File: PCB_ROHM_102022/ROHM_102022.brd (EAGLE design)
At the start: 152.4 x 142.2 mm, 126 parts, among them IC1 AMS1117-1.8, IC10 TXB0108PWR, IC2 TXB0108PWR, IC3 W9825G6KH-6I, IC4 AMS1117-1.8, IC5 AMS1117-1.8, IC7 TXB0108PWR, J1 2985-6004, J2 2985-6004, J3 2985-6004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

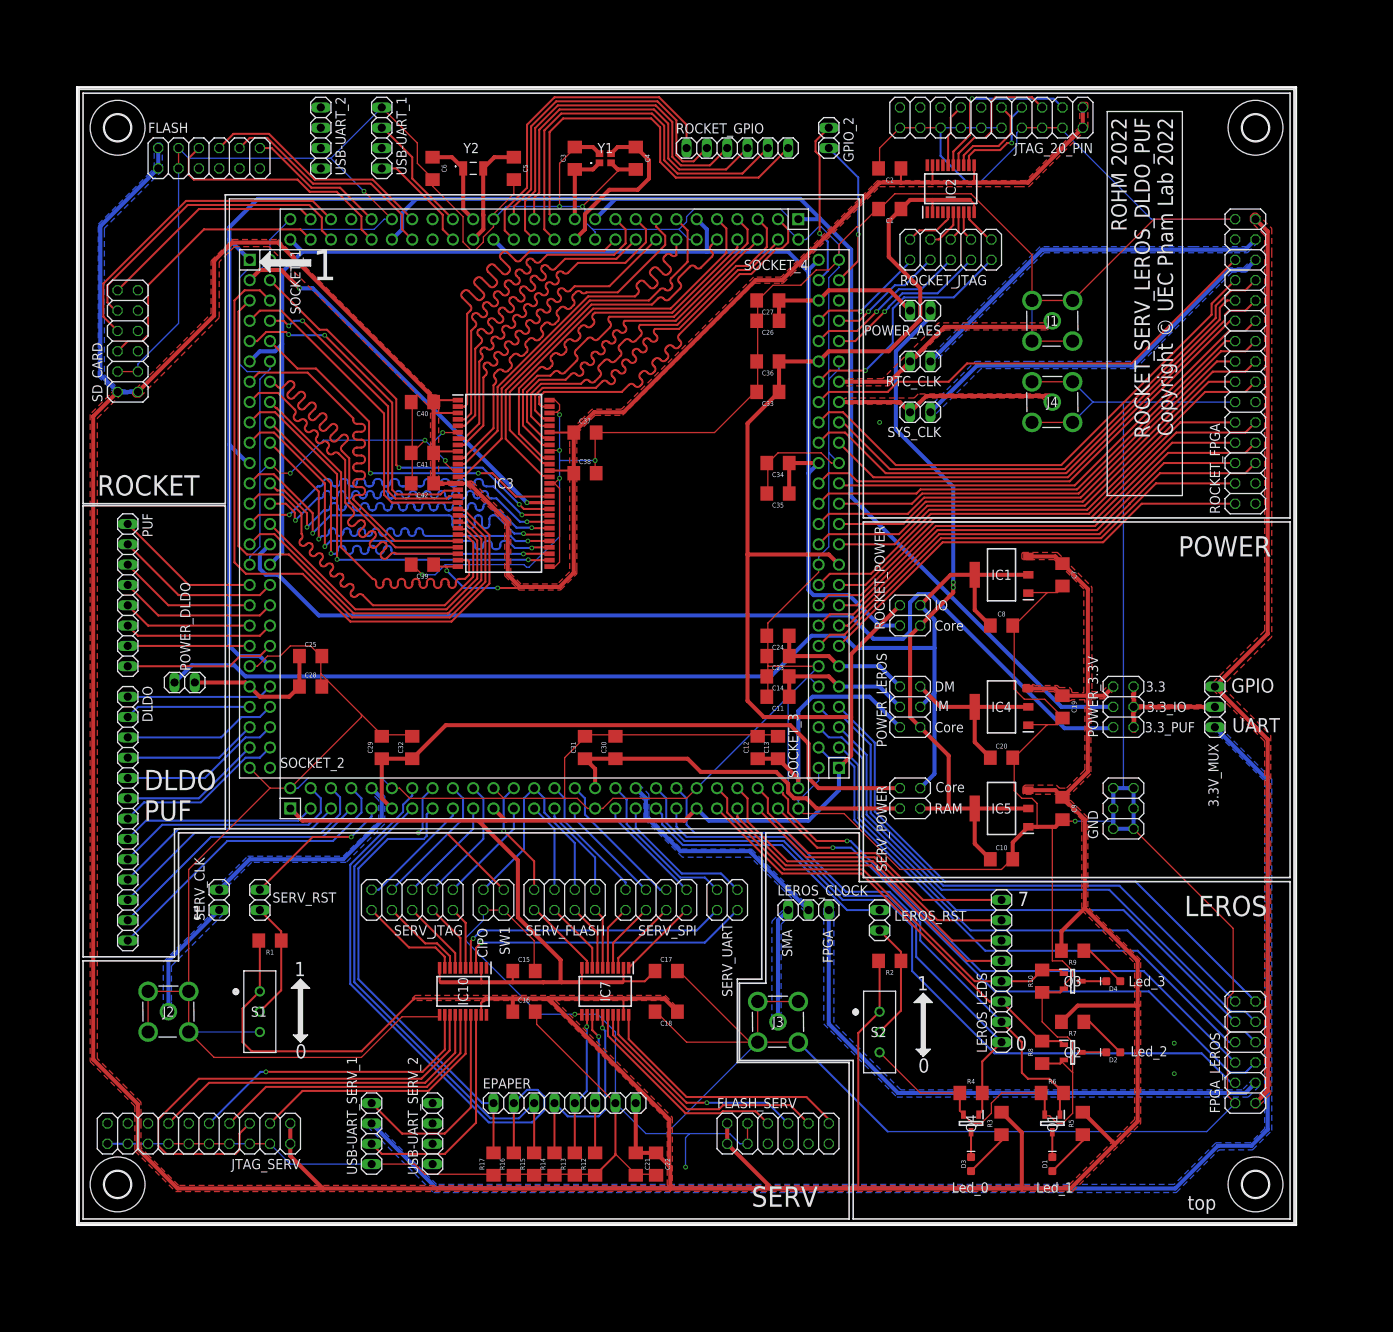
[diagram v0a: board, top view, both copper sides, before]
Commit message: Connect JTAG to FPGA
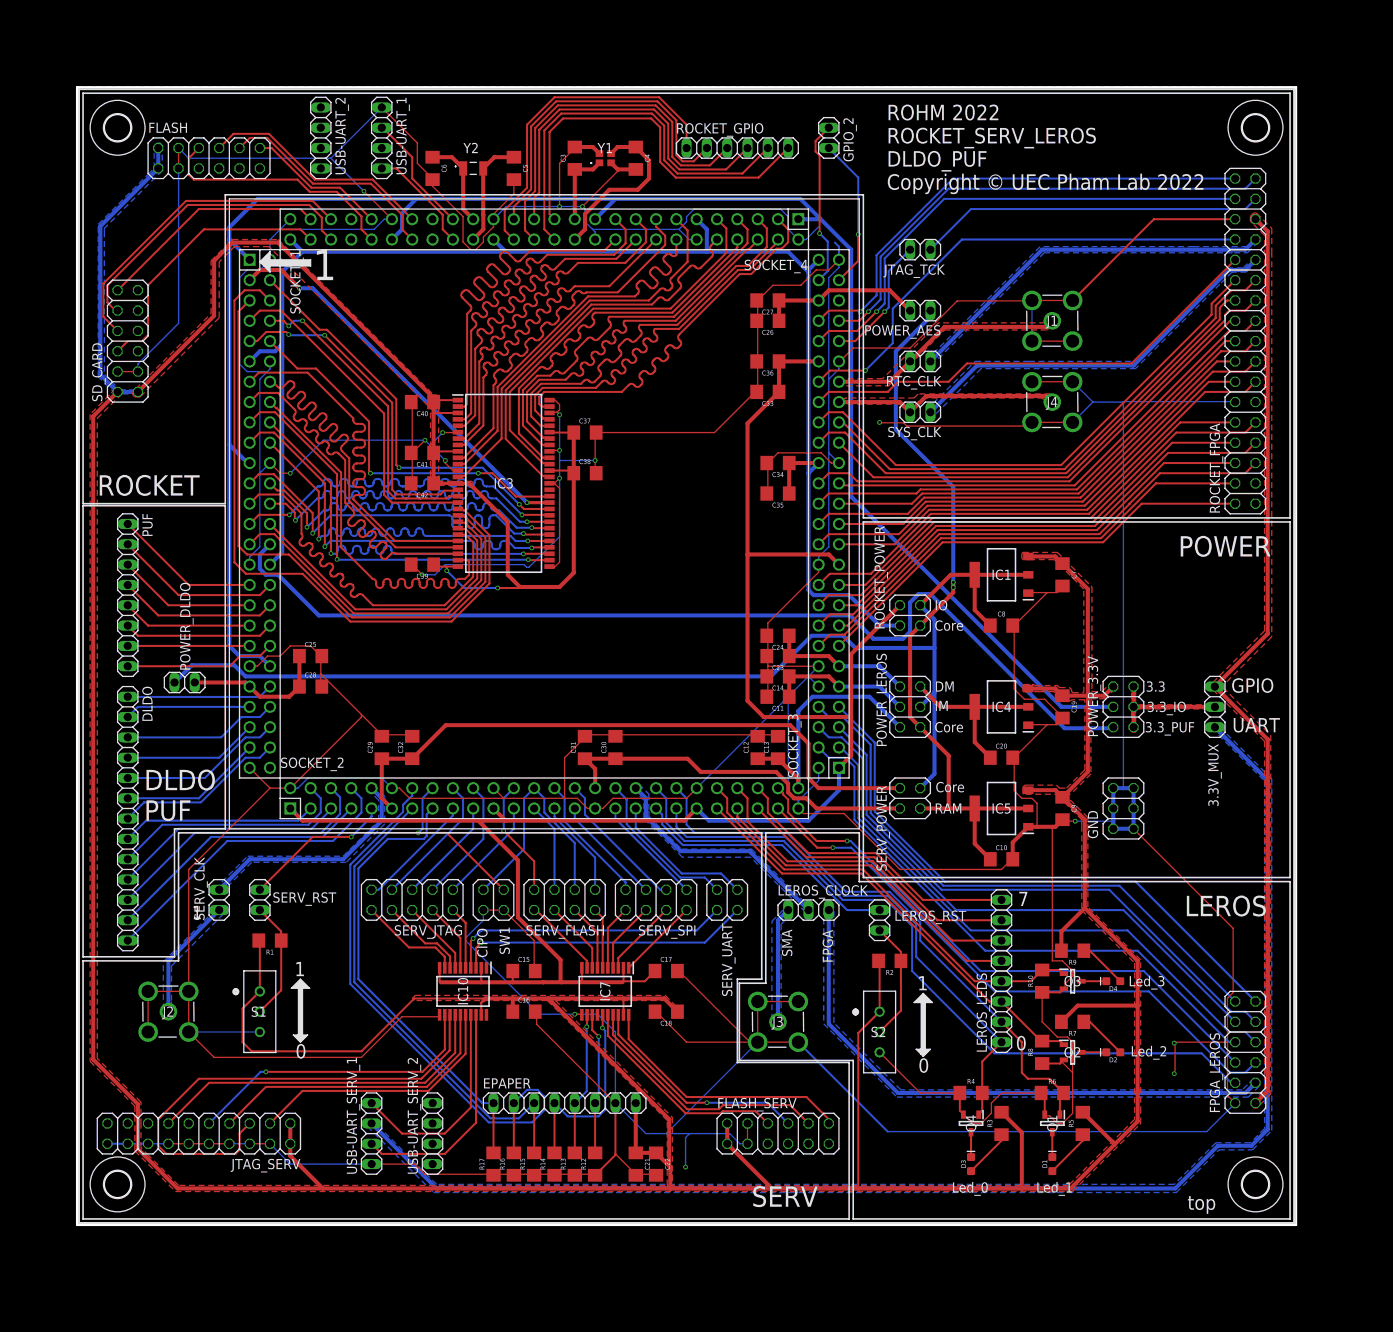
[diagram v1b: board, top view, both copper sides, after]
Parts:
- removed C1, C2: 0.1uF, SparkFun-Capacitors:1206
- removed IC2: TXB0108PWR, SamacSys_Parts:SOP65P640X120-20N
- removed JTAG_20_PIN: (no value), pinhead:2X10
- removed ROCKET_JTAG: PINHD-2X5, Connector:2X05
- added JTAG_TCK: (no value), pinhead:1X02
- ROCKET_FPGA: device pinhead:2X15 -> pinhead:2X17
- moved ROCKET_FPGA 2.54 mm to (87.6, 21.6)
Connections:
- removed net N$2: IC2.9, ROCKET_JTAG.10
- removed net N$6: IC2.8, ROCKET_JTAG.8
- removed net N$7: IC2.7, ROCKET_JTAG.6
- removed net N$8: IC2.6, ROCKET_JTAG.4
- removed net N$9: IC2.5, ROCKET_JTAG.2
- removed net TDI: IC2.14, JTAG_20_PIN.5
- removed net TDO: IC2.16, JTAG_20_PIN.13
- removed net TMS: IC2.12, JTAG_20_PIN.7
- removed net TRSTN: IC2.15, JTAG_20_PIN.3
- net GND: no longer C1.2, C2.2, JTAG_20_PIN.10, JTAG_20_PIN.12, JTAG_20_PIN.14, JTAG_20_PIN.16, JTAG_20_PIN.18, JTAG_20_PIN.20, JTAG_20_PIN.4, JTAG_20_PIN.6, JTAG_20_PIN.8
- net JTAG_TCK: now also JTAG_TCK.1; no longer ROCKET_JTAG.7
- net JTAG_TDI: now also ROCKET_FPGA.32; no longer ROCKET_JTAG.5
- net JTAG_TDO: now also ROCKET_FPGA.34; no longer ROCKET_JTAG.1
- net JTAG_TMS: now also ROCKET_FPGA.28; no longer ROCKET_JTAG.9
- net JTAG_TRSTN: now also ROCKET_FPGA.33; no longer ROCKET_JTAG.3
- net TCK: now also JTAG_TCK.2, ROCKET_FPGA.31; no longer IC2.13, JTAG_20_PIN.9
- net VDD_1.8_IO: no longer C1.1, IC2.10, IC2.2
- net VDD_3V3: no longer C2.1, IC2.11, IC2.19, JTAG_20_PIN.1, JTAG_20_PIN.2
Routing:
- net VDD_3V3: track 794.3 -> 706.2 mm
- net GND: track 1514.9 -> 1462.4 mm
- net JTAG_TRSTN: track 14.6 -> 62.6 mm
- net JTAG_TDO: track 14.8 -> 62.5 mm
- net VDD_1.8_IO: track 279.1 -> 235.7 mm
- net JTAG_TDI: track 20.7 -> 62.7 mm
- net JTAG_TMS: track 30.4 -> 62.0 mm
- net TCK: track 12.0 -> 43.3 mm
- net TRSTN: track 21.0 -> 0.00 mm, vias 1 -> 0
- net TDI: track 17.6 -> 0.00 mm
- net TMS: track 12.1 -> 0.00 mm, vias 1 -> 0
- net TDO: track 7.88 -> 0.00 mm
- net N$9: track 6.67 -> 0.00 mm
- net N$8: track 5.22 -> 0.00 mm
- net N$2: track 4.72 -> 0.00 mm
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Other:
- board text added: "ROHM 2022 ROCKET_SERV_LEROS DLDO_PUF Copyright © UEC Pham Lab 2022"
- board text removed: "ROHM 2022 ROCKET_SERV_LEROS_DLDO_PUF Copyright © UEC Pham Lab 2022"

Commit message: Upload bom and cpl
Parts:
- removed D1, D2, D3, D4: LED0, SparkFun-LED:LED-0603
- removed JTAG_TCK: (no value), pinhead:1X02
- removed Q1, Q2, Q3, Q4: BSH103,235, SamacSys_Parts:SOT95P230X110-3N
- removed R10, R12, R13, R15, R16, R17, R8: 10k, SparkFun-Resistors:1206
- removed R7, R9: 330, SparkFun-Resistors:1206
- added J5: (no value), SparkFun-Connectors:1X03
- added J6: (no value), SparkFun-Connectors:2X5
- added JP1: (no value), pinhead:1X03
- added JTAG_ROCKET: (no value), pinhead:2X10
- added LED1, LED2, LED3, LED4, LOADED: (no value), adafruit:CHIPLED_0805
- added R11: 10k, SparkFun-Resistors:1206
- added S3: SS12SDP2, SamacSys_Parts:SS12SDP2
- R14, R4, R6: value 10k -> 330; device SparkFun-Resistors:1206 -> Resistor:RESC3216X70
- R3, R5: device SparkFun-Resistors:1206 -> Resistor:RESC3216X70
- moved R14 49.6 mm to (50.8, -78.7)
- moved R6 25.0 mm to (73.7, -49.5)
- moved R4 9.92 mm to (61.0, -78.7), turned to 90 degrees
- moved R3 2.84 mm to (55.9, -78.7)
- moved R5 2.84 mm to (66.0, -78.7)
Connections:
- removed net N$16: D1.A, R5.1
- removed net N$17: D1.C, Q1.3
- removed net N$18: D2.A, R7.1
- removed net N$19: D2.C, Q2.3
- removed net N$20: D4.A, R9.1
- removed net N$21: D4.C, Q3.3
- removed net TCK: JTAG_TCK.2, ROCKET_FPGA.31
- new net JTAG_TCK_FPGA: J6.3, ROCKET_FPGA.31
- new net JTAG_TDI_FPGA: J6.5, ROCKET_FPGA.32
- new net JTAG_TDO_FPGA: J6.9, ROCKET_FPGA.34
- new net JTAG_TMS_FPGA: J6.1, ROCKET_FPGA.28
- new net JTAG_TRSTN_FPGA: J6.7, ROCKET_FPGA.33
- new net LEROS_PAD_LOADER_RST_N_0_FPGA: FPGA_LEROS.4, JP1.1
- new net LEROS_PAD_SRAM_LOADED_0_FPGA: FPGA_LEROS.12, J5.1
- new net N$2: LED1.C, R14.2
- new net N$6: JP1.3, R11.1, S3.2
- new net N$7: LED2.C, R3.2
- new net N$8: LED3.C, R4.2
- new net N$9: LED4.C, R5.2
- net GND: now also JTAG_ROCKET.10, JTAG_ROCKET.12, JTAG_ROCKET.14, JTAG_ROCKET.16, JTAG_ROCKET.18, JTAG_ROCKET.20, JTAG_ROCKET.4, JTAG_ROCKET.6, JTAG_ROCKET.8, R3.1, R5.1, S3.3; no longer Q1.2, Q2.2, Q3.2, Q4.2, R10.1, R12.1, R13.1, R15.1, R16.1, R17.1, R8.1
- net JTAG_TCK: now also J6.4, JTAG_ROCKET.9; no longer JTAG_TCK.1
- net JTAG_TDI: now also J6.6, JTAG_ROCKET.5; no longer ROCKET_FPGA.32
- net JTAG_TDO: now also J6.10, JTAG_ROCKET.13; no longer ROCKET_FPGA.34
- net JTAG_TMS: now also J6.2, JTAG_ROCKET.7; no longer ROCKET_FPGA.28
- net JTAG_TRSTN: now also J6.8, JTAG_ROCKET.3; no longer ROCKET_FPGA.33
- net LEROS_PAD_LOADER_RST_N_0: now also JP1.2; no longer FPGA_LEROS.4
- net LEROS_PAD_OLEDG_0_0: now also LED1.A; no longer Q4.1, R4.2
- net LEROS_PAD_OLEDG_0_1: now also LED2.A; no longer Q1.1, R6.2
- net LEROS_PAD_OLEDG_0_2: now also LED3.A; no longer Q2.1, R8.2
- net LEROS_PAD_OLEDG_0_3: now also LED4.A; no longer Q3.1, R10.2
- net LEROS_PAD_SRAM_LOADED_0: now also J5.2; no longer FPGA_LEROS.12
- net N$14: now also LOADED.C, R6.2; no longer D3.C, Q4.3
- net N$15: now also J5.3, LOADED.A; no longer D3.A, R3.1
- net SERV_MOD_IO_ALL_DIPSW_PAD_ALL_DIPSW_0_0: no longer R17.2
- net SERV_PAD_ALL_LEDS_0_0: no longer R15.2
- net SERV_PAD_ALL_LEDS_0_1: no longer R16.2
- net SERV_SPI_COPI: no longer R12.2
- net SERV_SPI_CS: no longer R14.2
- net SERV_SPI_SCK: no longer R13.2
- net VDD_3V3: now also JTAG_ROCKET.1, JTAG_ROCKET.2, R11.2, S3.1; no longer R3.2, R5.2, R7.2, R9.2
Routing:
- net GND: track 1462.4 -> 1609.0 mm, vias 18 -> 76
- net VDD_3V3: track 706.2 -> 804.5 mm
- net TCK: track 43.3 -> 0.00 mm
- net JTAG_TCK: track 16.3 -> 49.4 mm
- net JTAG_TCK_FPGA: track 0.00 -> 15.1 mm
- net JTAG_TRSTN_FPGA: track 0.00 -> 14.1 mm
- net N$6: track 0.00 -> 13.3 mm
- net JTAG_TRSTN: track 62.6 -> 50.8 mm
- net JTAG_TMS_FPGA: track 0.00 -> 11.5 mm
- net JTAG_TDI_FPGA: track 0.00 -> 11.5 mm
- net JTAG_TDO_FPGA: track 0.00 -> 10.5 mm
- net LEROS_PAD_LOADER_RST_N_0: track 92.7 -> 82.4 mm
- net JTAG_TDI: track 62.7 -> 52.8 mm
- net JTAG_TDO: track 62.5 -> 53.0 mm
- net LEROS_PAD_LOADER_RST_N_0_FPGA: track 0.00 -> 9.42 mm
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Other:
- board text added: "LED"
- board text added: "SW"
- board text removed: "Led_0"
- board text removed: "Led_1"
- board text removed: "Led_2"
- board text removed: "Led_3"
